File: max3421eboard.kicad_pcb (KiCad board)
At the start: 2 copper layers, 41.3 x 48.9 mm, 32 parts, among them J1 USB A, J2 USB MicroB, J3 1x10, J4 1x8, J5 1x8, J6 1x3, J7 Conn_01x04, U1 MAX3421E, U2 LP2985-3.3, U3 STMPS2141STR, Y1 12MHz

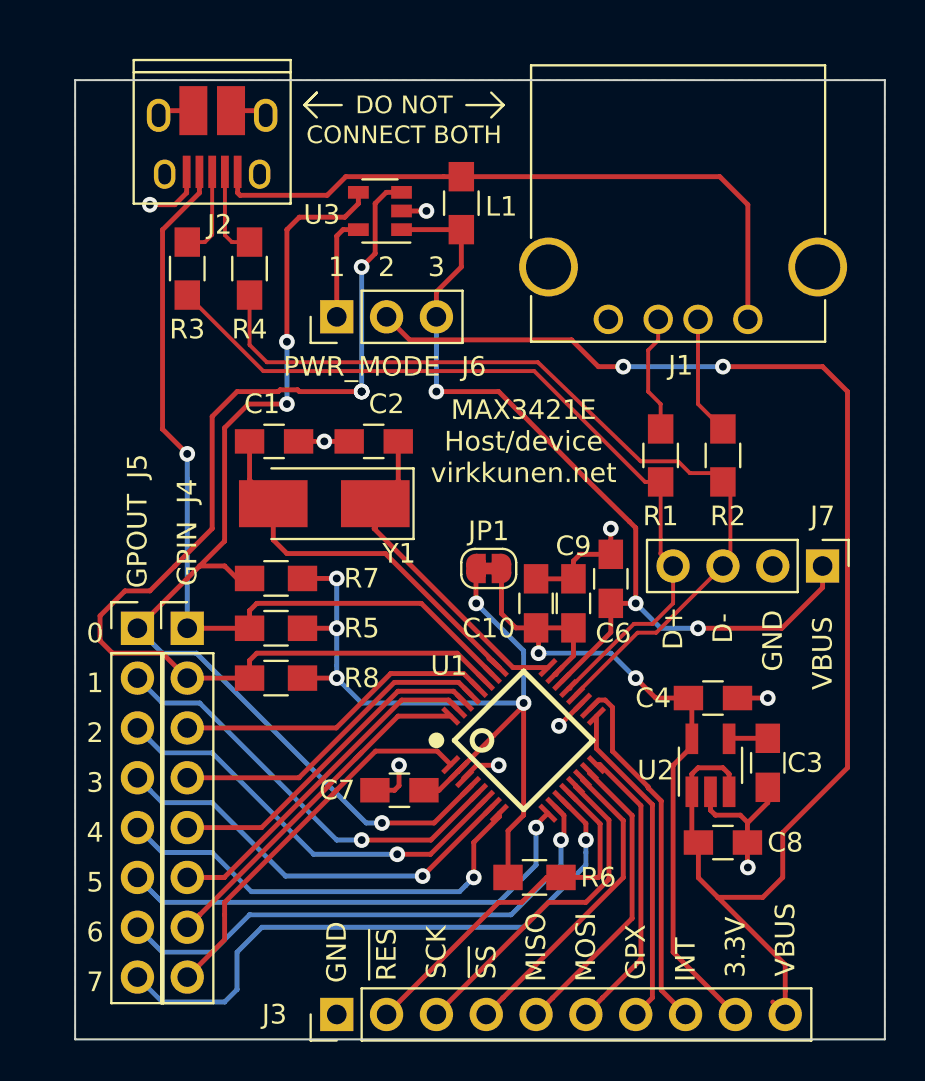
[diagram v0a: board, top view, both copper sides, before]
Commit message: Align board to the 1mm grid
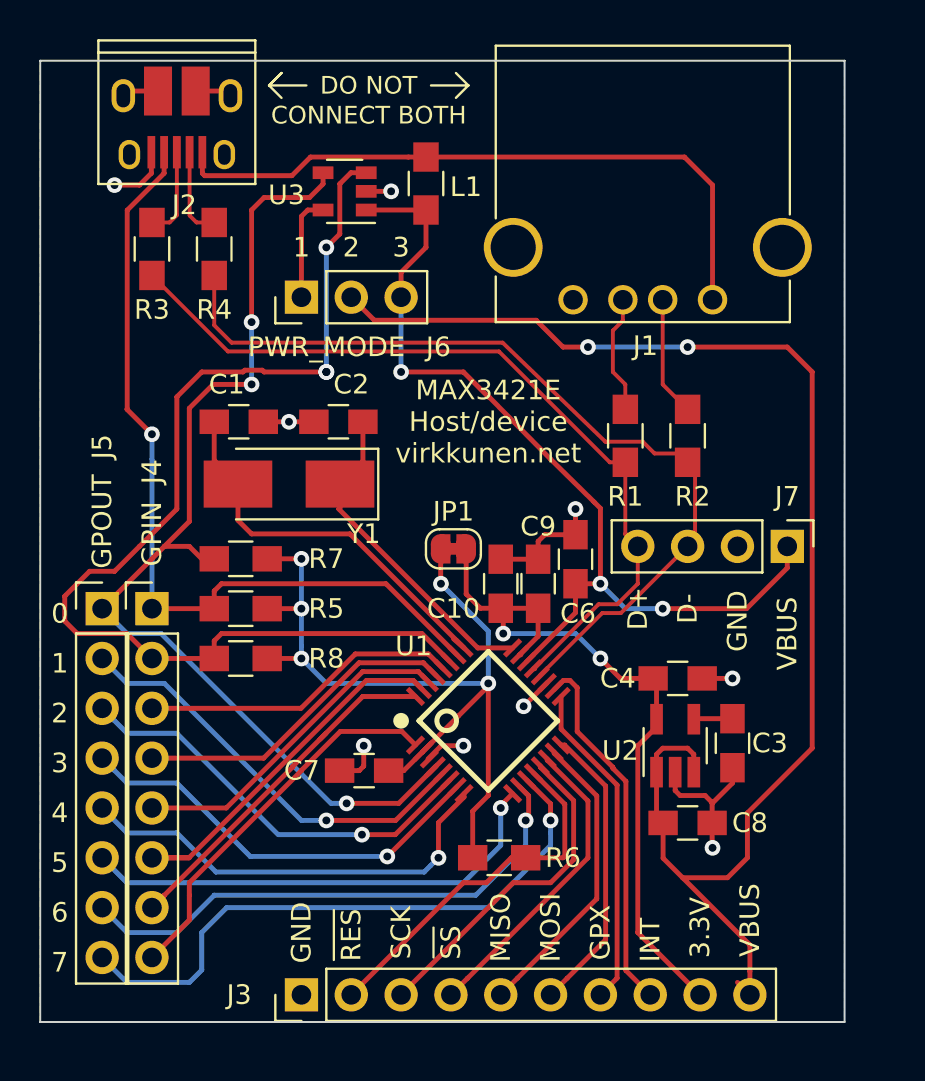
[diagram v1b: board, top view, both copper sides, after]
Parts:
- moved C4 2.06 mm to (48.5, 77.5)
- moved C6 2.06 mm to (43.3, 71.4)
- moved C7 2.06 mm to (32.5, 82.2)
- moved G*** 2.06 mm to (40.7, 90.4)
- moved J7 2.06 mm to (54.1, 70.8)
- moved JP1 2.06 mm to (37.1, 70.9)
- moved L1 2.06 mm to (35.7, 52.3)
- moved REF*** 2.06 mm to (43.3, 65.7)
- moved C1 2.06 mm to (26.1, 64.4)
- moved C2 2.06 mm to (31.2, 64.4)
- moved J2 2.06 mm to (23.0, 49.2)
- moved J4 2.06 mm to (21.7, 73.9)
- moved R3 2.06 mm to (21.7, 55.6)
- moved R4 2.06 mm to (24.9, 55.6)
- moved R5 2.06 mm to (26.2, 73.9)
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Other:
- board size 41.3 x 48.9 mm -> 41 x 49 mm
- rule pad_to_mask_clearance: 0.051 -> 0.05
- rule solder_mask_min_width: 0.25 -> 0.145

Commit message: Fix the board layout
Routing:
- net /X+: track 21.4 -> 20.7 mm
